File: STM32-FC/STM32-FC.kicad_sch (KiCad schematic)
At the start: 39 parts, among them J1 GH 1.25mm 6P, Q1 S9013, SW2 SW_DIP_x03, U1 STM32F407VETx, Y1 16MHz

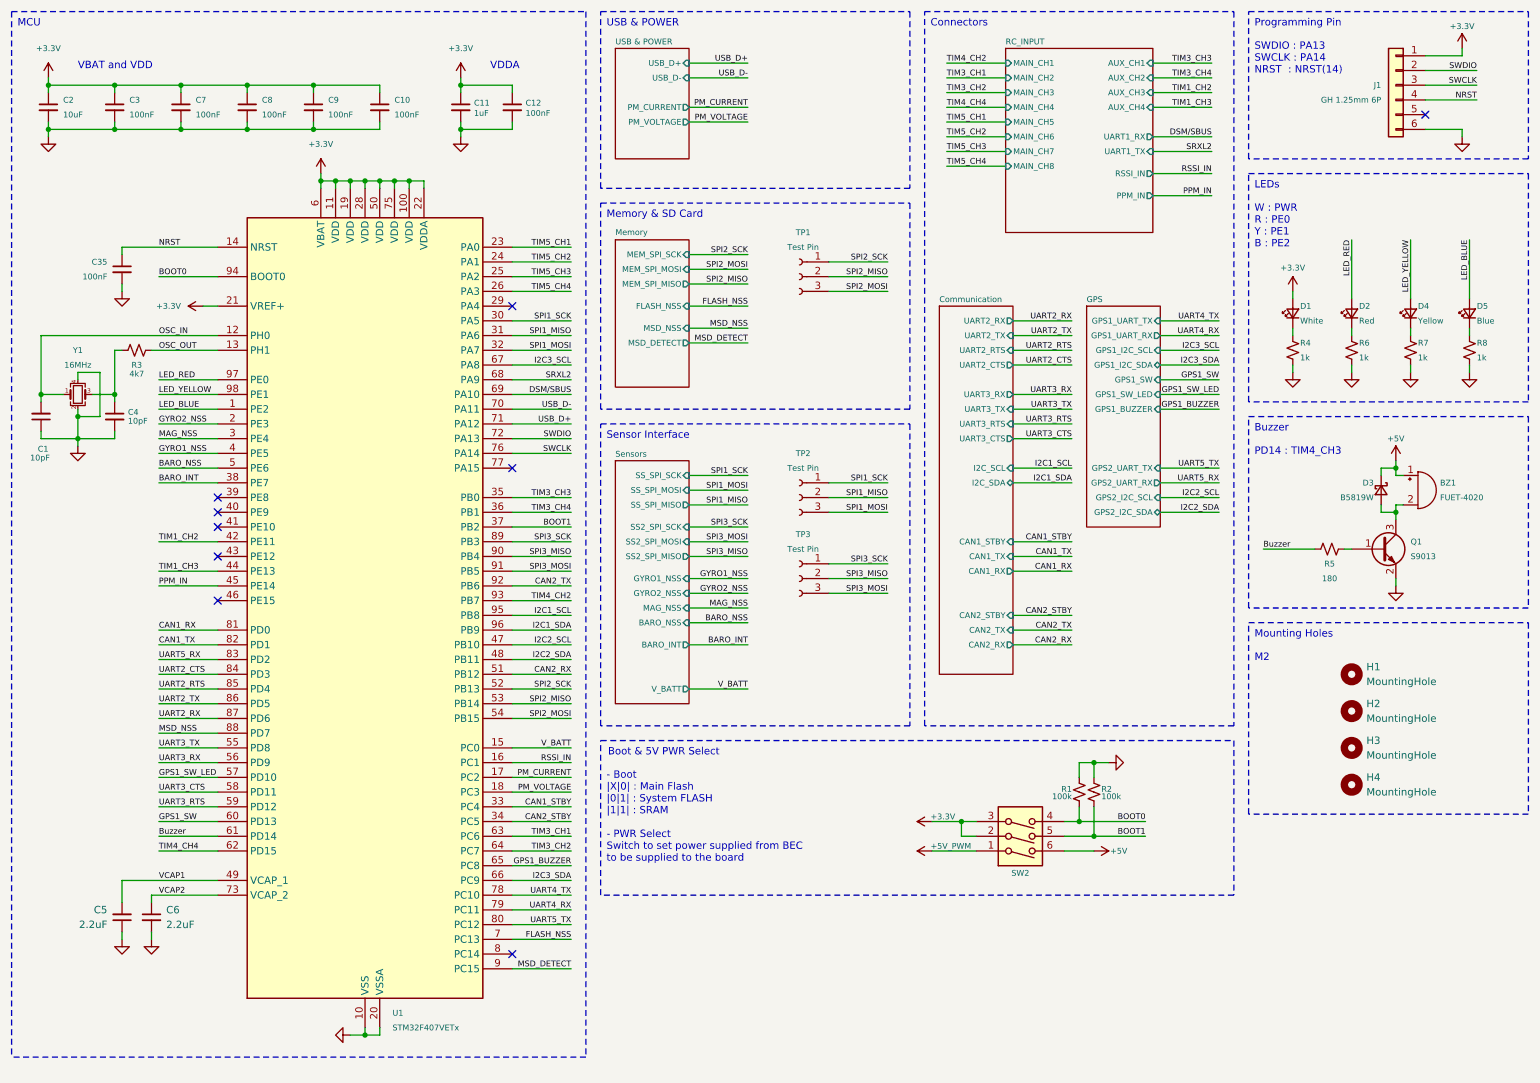
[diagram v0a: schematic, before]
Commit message: v1.0.1 update WIP
repactor and USB C bug fix
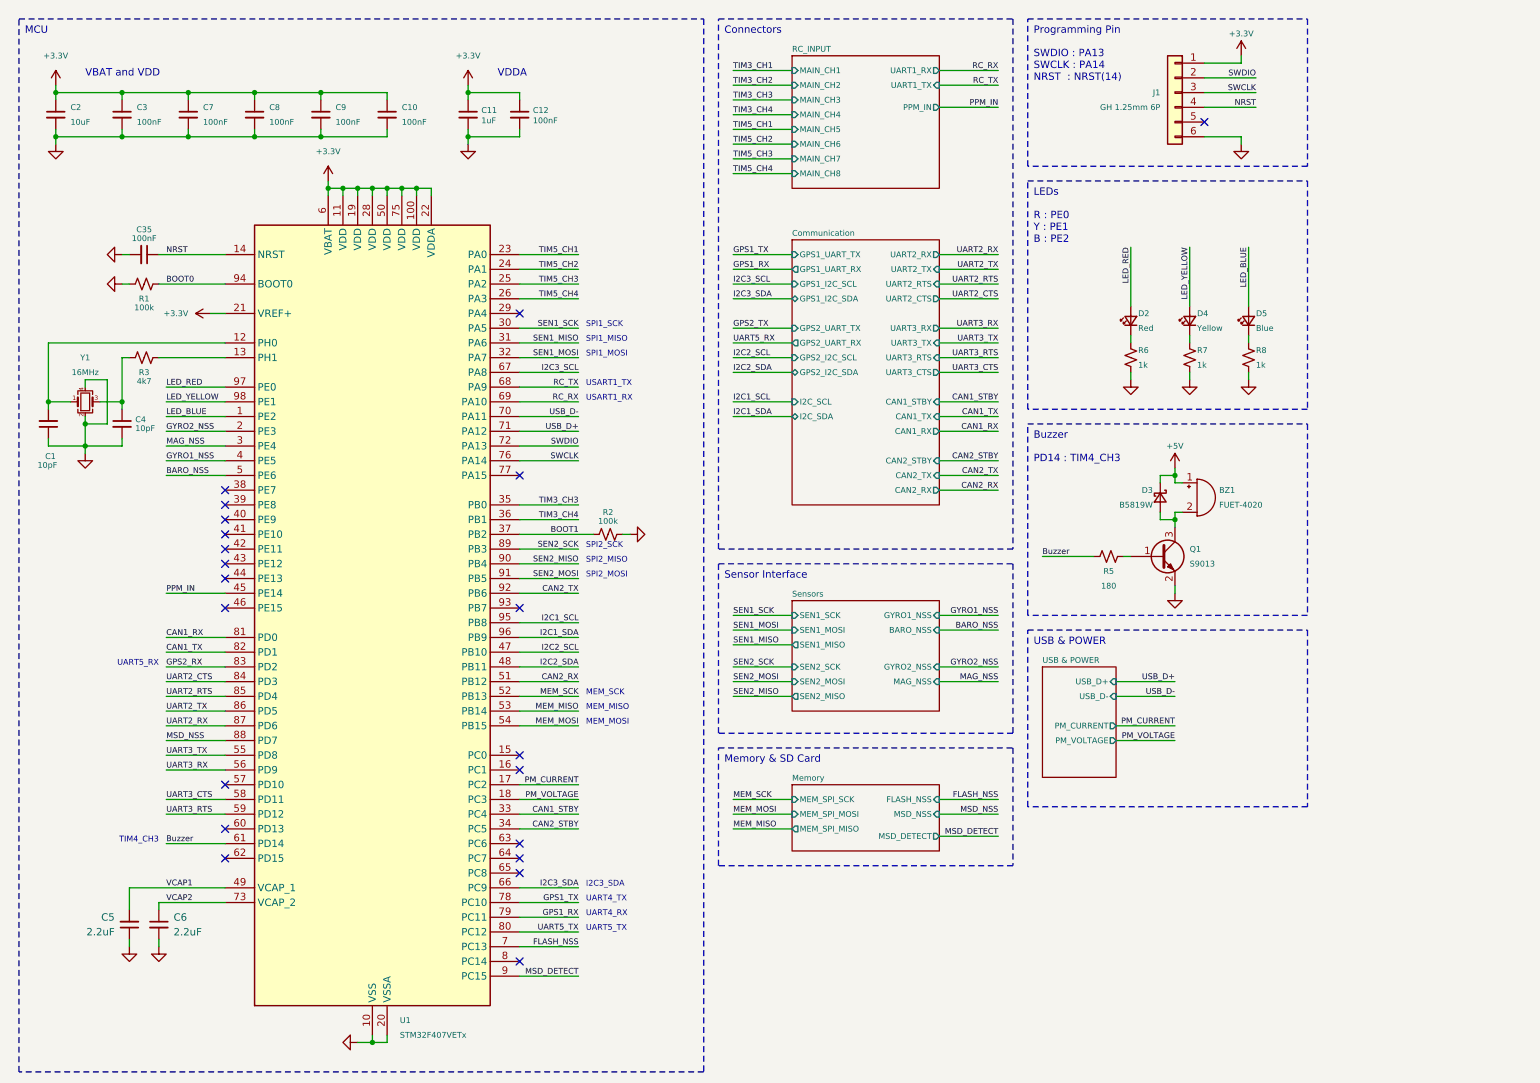
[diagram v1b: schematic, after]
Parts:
- removed D1: White, LED_SMD:LED_0402_1005Metric, symbol Device:LED_Small
- removed H1, H2, H3, H4: MountingHole, Hole:MountingHole_2.2mm_M2, symbol Mechanical:MountingHole
- removed R4: 1k, Resistor_SMD:R_0402_1005Metric, symbol Device:R_Small_US
- removed SW2: SW_DIP_x03, Button_Switch_SMD:SW_DIP_SPSTx03_Slide_KingTek_DSHP03TJ_W5.25mm_P1.27mm_JPin, symbol Switch:SW_DIP_x03
- removed TP1, TP2, TP3: Test Pin, Connector_PinHeader_1.27mm:PinHeader_1x03_P1.27mm_Vertical, symbol Connector:Conn_01x03_Socket
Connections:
- net TIM3_CH1: no longer U1.63 (PC6)
- net TIM3_CH2: no longer U1.64 (PC7)
- net UART5_RX: no longer U1.83 (PD2)
- net BARO_INT: no longer names the net of U1.38 (PE7)
- net DSM/SBUS renamed RC_RX
- net GPS1_BUZZER: no longer names the net of U1.65 (PC8)
- net GPS1_SW: no longer names the net of U1.60 (PD13)
- net GPS1_SW_LED: no longer names the net of U1.57 (PD10)
- net OSC_IN: no longer names the net of C1.2, U1.12 (PH0), Y1.1
- net OSC_OUT: no longer names the net of R3.2, U1.13 (PH1)
- net RSSI_IN: no longer names the net of U1.16 (PC1)
- net SPI1_MISO renamed SEN1_MISO
- net SPI1_MOSI renamed SEN1_MOSI
- net SPI1_SCK renamed SEN1_SCK
- net SPI2_MISO renamed MEM_MISO
- net SPI2_MOSI renamed MEM_MOSI
- net SPI2_SCK renamed MEM_SCK
- net SPI3_MISO renamed SEN2_MISO
- net SPI3_MOSI renamed SEN2_MOSI
- net SPI3_SCK renamed SEN2_SCK
- net SRXL2 renamed RC_TX
- net TIM1_CH2: no longer names the net of U1.42 (PE11)
- net TIM1_CH3: no longer names the net of U1.44 (PE13)
- net TIM4_CH2: no longer names the net of U1.93 (PB7)
- net TIM4_CH4: no longer names the net of U1.62 (PD15)
- net UART4_RX renamed GPS1_RX
- net UART4_TX renamed GPS1_TX
- net V_BATT: no longer names the net of U1.15 (PC0)
- new net GPS2_RX: U1.83 (PD2)
- no-connect marks 9 -> 21
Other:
- removed sheet GPS
- sheet Communication ports: added GPS1_I2C_SCL, GPS1_I2C_SDA, GPS1_UART_RX, GPS1_UART_TX, GPS2_I2C_SCL, GPS2_I2C_SDA, GPS2_UART_RX, GPS2_UART_TX; removed none
- sheet RC_INPUT ports: added none; removed AUX_CH1, AUX_CH2, AUX_CH3, AUX_CH4, RSSI_IN
- sheet Sensors ports: added SEN1_MISO, SEN1_MOSI, SEN1_SCK, SEN2_MISO, SEN2_MOSI, SEN2_SCK; removed BARO_INT, SS2_SPI_MISO, SS2_SPI_MOSI, SS2_SPI_SCK, SS_SPI_MISO, SS_SPI_MOSI, SS_SPI_SCK, V_BATT
- note added: "I2C3_SDA"
- note added: "MEM_MISO"
- note added: "MEM_MOSI"
- note added: "MEM_SCK"
- note added: "R : PE0 Y : PE1 B : PE2"
- note added: "SPI1_MISO"
- note added: "SPI1_MOSI"
- note added: "SPI1_SCK"
- note added: "SPI2_MISO"
- note added: "SPI2_MOSI"
- note added: "SPI2_SCK"
- note added: "TIM4_CH3"
- note added: "UART4_RX"
- note added: "UART4_TX"
- note added: "UART5_RX"
- note added: "UART5_TX"
- note added: "USART1_RX"
- note added: "USART1_TX"
- note removed: "- Boot |X|0| : Main Flash |0|1| : System FLASH |1|1| : SRAM - PWR Select Switch to set power supplied from BEC to be supplied to the board"
- note removed: "Boot & 5V PWR Select"
- note removed: "M2"
- note removed: "Mounting Holes"
- note removed: "W : PWR R : PE0 Y : PE1 B : PE2"
- moved on the sheet: BZ1, C1, C10, C11, C12, C2, C3, C35, C4, C5, C6, C7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

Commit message: schematic update & lib update
- ICM-45686
- ICP-20100
- Micro SD update SDIO instead of SPI
- servo main output
- DC2DC buck instead power regulator
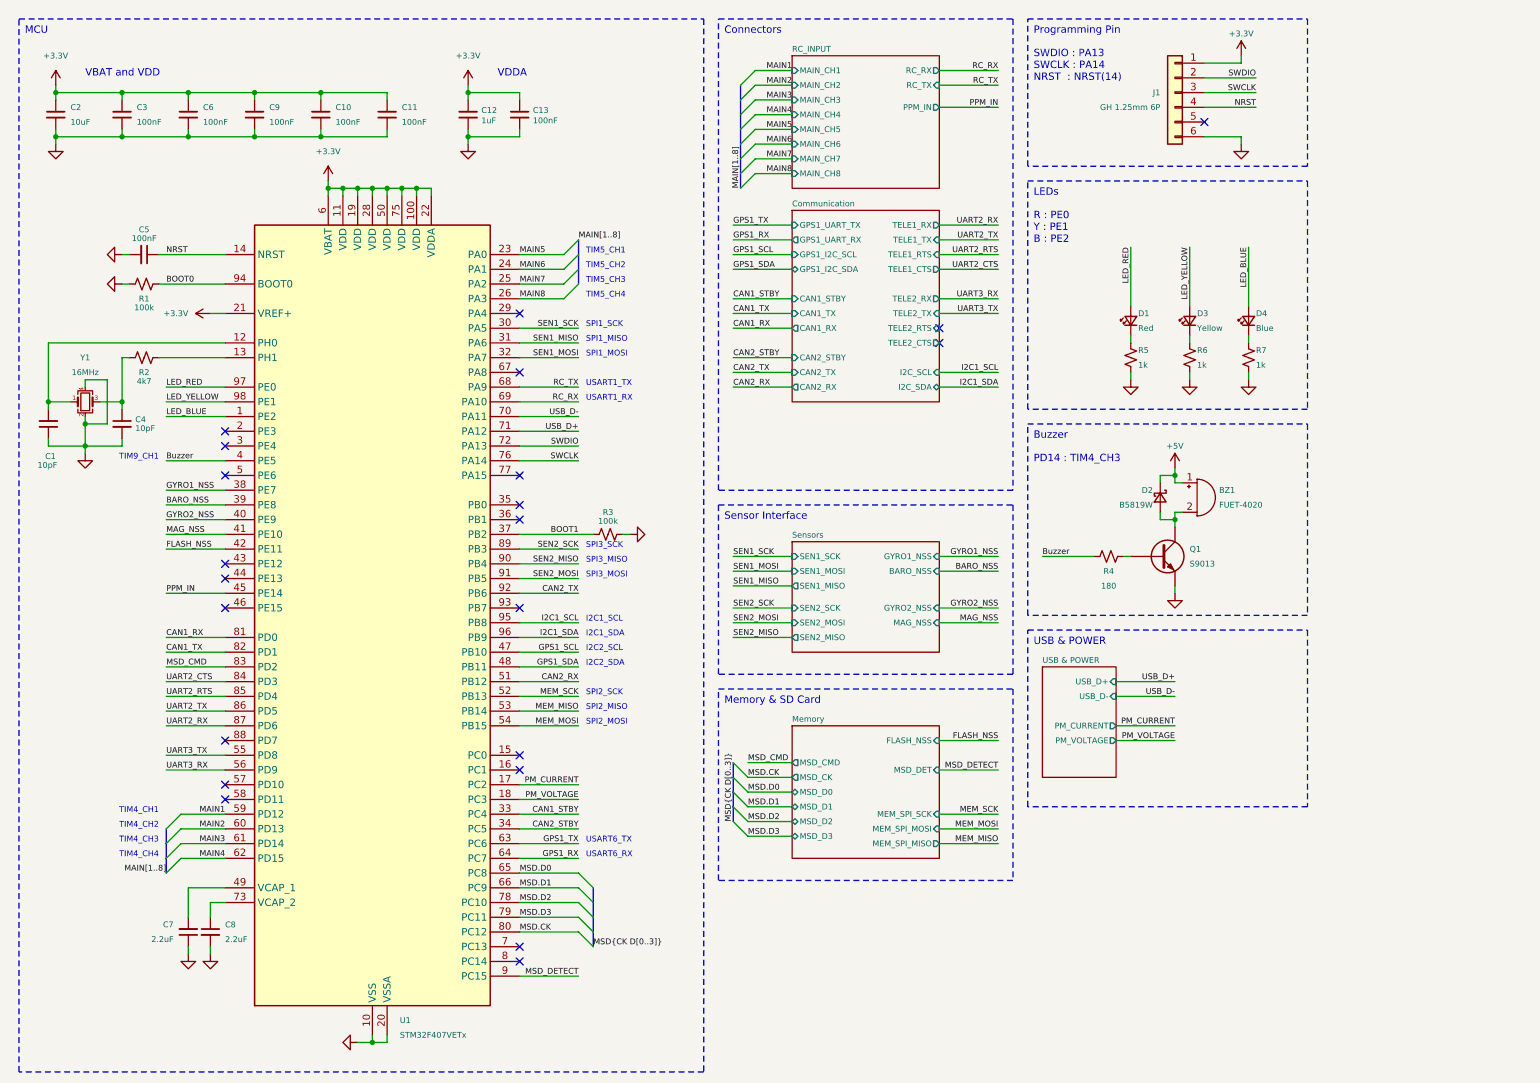
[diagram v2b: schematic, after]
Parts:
- C2: LCSC C77000 -> C307415
- J1: footprint JST_GH:JST_GH_SM06B-GHS-TB_06x1.25mm_Angled -> Connector_JST:JST_GH_BM06B-GHS-TBT_1x06-1MP_P1.25mm_Vertical; LCSC C133065 -> C189892
- Q1: symbol Device:Q_NPN_BEC -> Device:Q_NPN
- renumbered C9 to C10, C10 to C11, C11 to C12, C12 to C13, C35 to C5, C7 to C6, C5 to C7, C6 to C8, C8 to C9, D2 to D1, D3 to D2, D4 to D3, D5 to D4, R3 to R2, R2 to R3, R5 to R4, R6 to R5, R7 to R6, R8 to R7
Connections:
- net BARO_NSS: now also U1.39 (PE8); no longer U1.5 (PE6)
- net Buzzer: now also U1.4 (PE5); no longer U1.61 (PD14)
- net FLASH_NSS: now also U1.42 (PE11); no longer U1.7 (PC13)
- net GND: now also Q1.E; no longer Q1.2 (E)
- net GPS1_RX: now also U1.64 (PC7); no longer U1.79 (PC11)
- net GPS1_TX: now also U1.63 (PC6); no longer U1.78 (PC10)
- net GYRO1_NSS: now also U1.38 (PE7); no longer U1.4 (PE5)
- net GYRO2_NSS: now also U1.40 (PE9); no longer U1.2 (PE3)
- net MAG_NSS: now also U1.41 (PE10); no longer U1.3 (PE4)
- net at R4.2: now also Q1.B; no longer Q1.1 (B)
- net at BZ1.2 (+), D2.2 (A): now also Q1.C; no longer Q1.3 (C)
- net MAIN2: now reaches U1.60 (PD13)
- net MAIN4: now reaches U1.62 (PD15)
- net MSD.D0: now reaches U1.65 (PC8)
- net GPS2_RX renamed MSD_CMD
- net I2C2_SCL renamed GPS1_SCL
- net I2C2_SDA renamed GPS1_SDA
- net I2C3_SCL: no longer names the net of U1.67 (PA8)
- net I2C3_SDA renamed MSD.D1
- net MSD_NSS: no longer names the net of U1.88 (PD7)
- net TIM3_CH3: no longer names the net of U1.35 (PB0)
- net TIM3_CH4: no longer names the net of U1.36 (PB1)
- net TIM5_CH1 renamed MAIN5
- net TIM5_CH2 renamed MAIN6
- net TIM5_CH3 renamed MAIN7
- net TIM5_CH4 renamed MAIN8
- net UART3_CTS: no longer names the net of U1.58 (PD11)
- net UART3_RTS renamed MAIN1
- net UART5_TX renamed MSD.CK
- net VCAP1: no longer names the net of C7.2, U1.49 (VCAP_1)
- net VCAP2: no longer names the net of C8.1, U1.73 (VCAP_2)
- new net MAIN3: U1.61 (PD14)
- new net MSD.D2: U1.78 (PC10)
- new net MSD.D3: U1.79 (PC11)
- no-connect marks 21 -> 22
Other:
- sheet Communication ports: added TELE1_CTS, TELE1_RTS, TELE1_RX, TELE1_TX, TELE2_CTS, TELE2_RTS, TELE2_RX, TELE2_TX; removed GPS2_I2C_SCL, GPS2_I2C_SDA, GPS2_UART_RX, GPS2_UART_TX, UART2_CTS, UART2_RTS, UART2_RX, UART2_TX, UART3_CTS, UART3_RTS, UART3_RX, UART3_TX
- sheet Memory ports: added MSD_CK, MSD_CMD, MSD_D0, MSD_D1, MSD_D2, MSD_D3, MSD_DET; removed MSD_DETECT, MSD_NSS
- sheet RC_INPUT ports: added RC_RX, RC_TX; removed UART1_RX, UART1_TX
- note added: "I2C1_SCL"
- note added: "I2C1_SDA"
- note added: "I2C2_SCL"
- note added: "I2C2_SDA"
- note added: "SPI3_MISO"
- note added: "SPI3_MOSI"
- note added: "SPI3_SCK"
- note added: "TIM4_CH1"
- note added: "TIM4_CH2"
- note added: "TIM4_CH4"
- note added: "TIM5_CH1"
- note added: "TIM5_CH2"
- note added: "TIM5_CH3"
- note added: "TIM5_CH4"
- note added: "TIM9_CH1"
- note added: "USART6_RX"
- note added: "USART6_TX"
- note removed: "I2C3_SDA"
- note removed: "MEM_MISO"
- note removed: "MEM_MOSI"
- note removed: "MEM_SCK"
- note removed: "UART4_RX"
- note removed: "UART4_TX"
- note removed: "UART5_RX"
- note removed: "UART5_TX"
- company: NARAE -> NARAE UAV Project 
- title: STM32 Flight Controller -> NARAEON - Flight Controller
- moved on the sheet: C7, C8

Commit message: add: servo power & comment
- Servo power diode add
- comment update
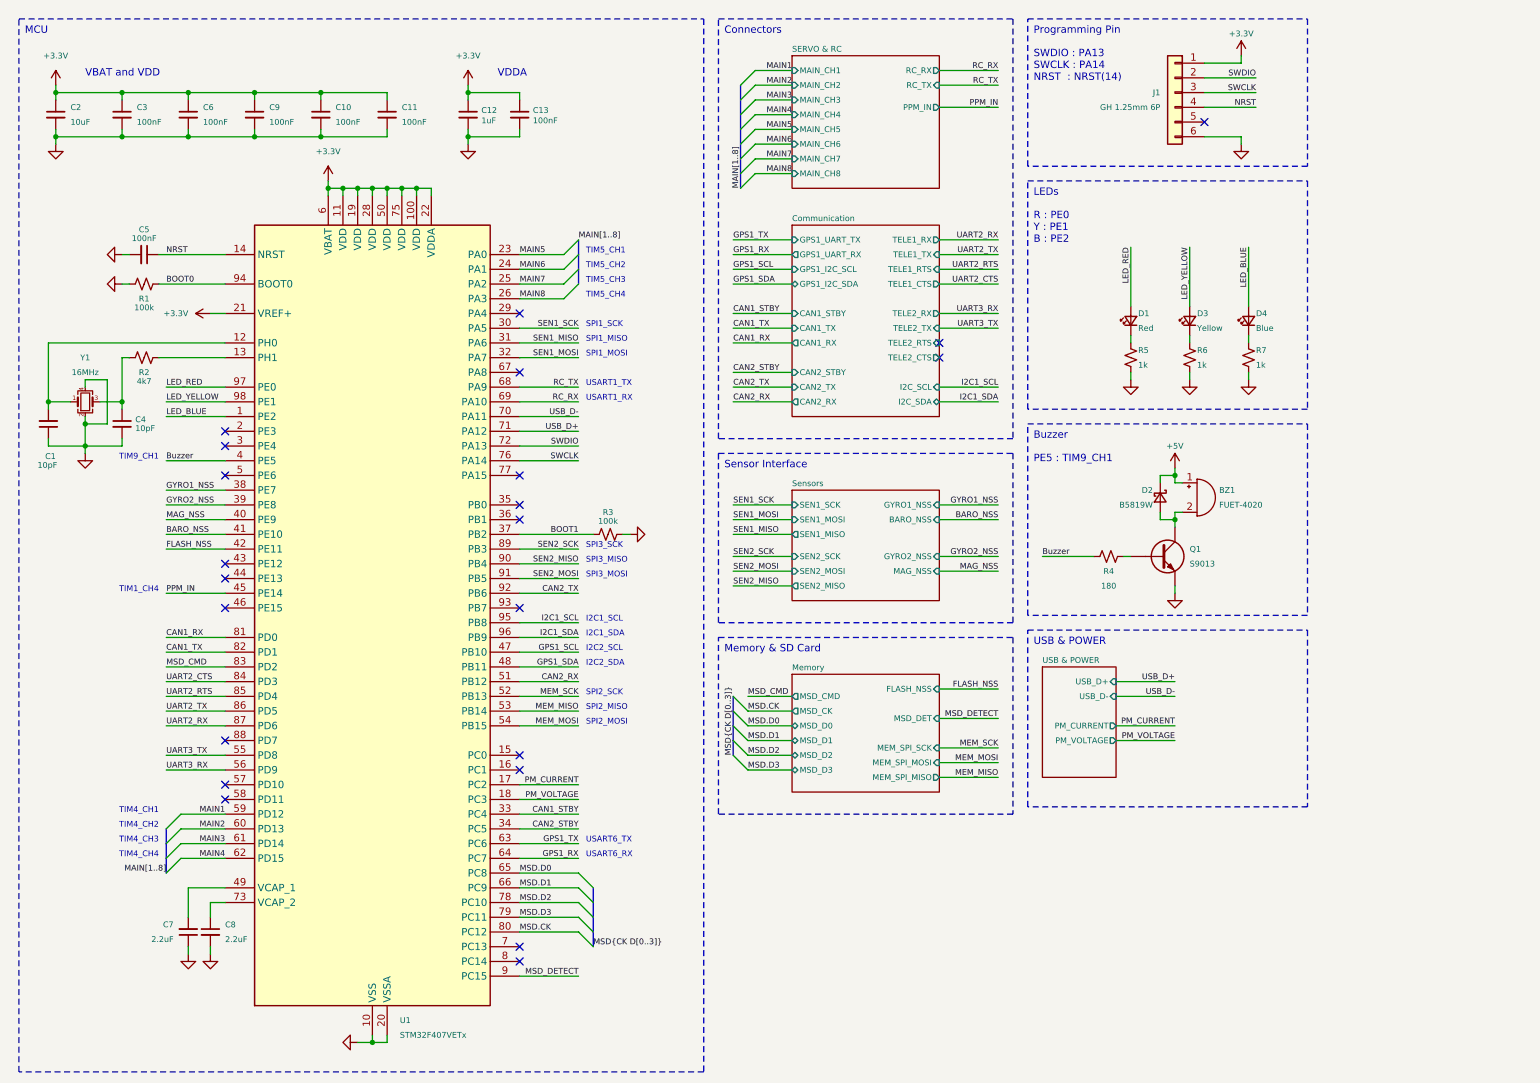
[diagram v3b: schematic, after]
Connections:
- net BARO_NSS: now also U1.41 (PE10); no longer U1.39 (PE8)
- net GYRO2_NSS: now also U1.39 (PE8); no longer U1.40 (PE9)
- net MAG_NSS: now also U1.40 (PE9); no longer U1.41 (PE10)
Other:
- sheet RC_INPUT renamed SERVO & RC
- sheet SERVO & RC: file schematic/io_RC_INPUT.kicad_sch -> schematic/io_SERVO_RC.kicad_sch
- note added: "PE5 : TIM9_CH1"
- note added: "TIM1_CH4"
- note removed: "PD14 : TIM4_CH3"
